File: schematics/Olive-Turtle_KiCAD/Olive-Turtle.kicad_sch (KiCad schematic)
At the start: 12 parts, among them IC1 ENS160-BGLT, U1 ESP32-DEVKITC-32U

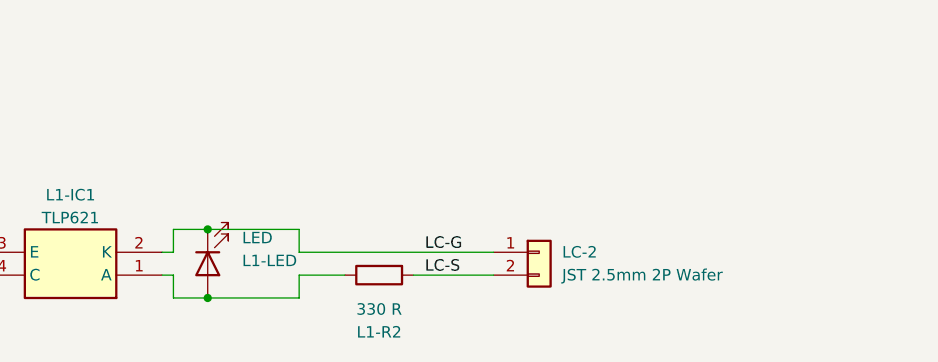
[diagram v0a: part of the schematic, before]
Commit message: [develop] Removed LED from LED Control circuit
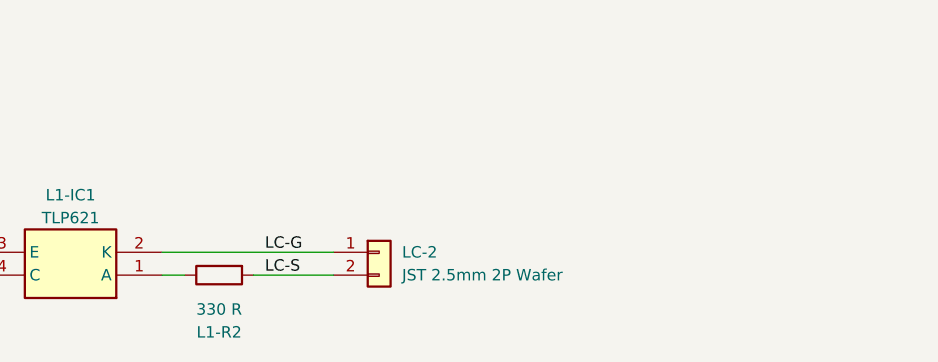
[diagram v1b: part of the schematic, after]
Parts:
- removed L1-LED: LED, symbol Device:LED
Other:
- moved on the sheet: L1-R2, LC-2
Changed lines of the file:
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@@
     (title "Olive Turtle Project - Led Control")
     (date "2023-09-21")
-    (rev "2.1")
+    (rev "2.2")
   )
   (junction (at 191.77 43.18) (diameter 0) (color 0 0 0 0)
   )
-  (junction (at 99.06 156.21) (diameter 0) (color 0 0 0 0)
-  )
   (junction (at 41.91 132.08) (diameter 0) (color 0 0 0 0)
-  )
-  (junction (at 99.06 148.59) (diameter 0) (color 0 0 0 0)
   )
   (junction (at 220.98 68.58) (diameter 0) (color 0 0 0 0)
@@
     (stroke (width 0) (type default))
   )
-  (wire (pts (xy 93.98 153.67) (xy 95.25 153.67))
-    (stroke (width 0) (type default))
-  )
   (wire (pts (xy 44.45 120.65) (xy 44.45 158.75))
     (stroke (width 0) (type default))
@@
     (stroke (width 0) (type default))
   )
-  (wire (pts (xy 114.3 153.67) (xy 109.22 153.67))
+  (wire (pts (xy 93.98 153.67) (xy 96.52 153.67))
     (stroke (width 0) (type default))
   )
@@
     (stroke (width 0) (type default))
   )
-  (wire (pts (xy 95.25 151.13) (xy 95.25 148.59))
-    (stroke (width 0) (type default))
-  )
   (wire (pts (xy 166.37 81.28) (xy 194.31 81.28))
     (stroke (width 0) (type default))
@@
     (stroke (width 0) (type default))
   )
-  (wire (pts (xy 121.92 153.67) (xy 130.81 153.67))
+  (wire (pts (xy 104.14 153.67) (xy 113.03 153.67))
     (stroke (width 0) (type default))
   )
@@
     (stroke (width 0) (type default))
   )
-  (wire (pts (xy 95.25 156.21) (xy 99.06 156.21))
-    (stroke (width 0) (type default))
-  )
-  (wire (pts (xy 130.81 151.13) (xy 109.22 151.13))
+  (wire (pts (xy 93.98 151.13) (xy 113.03 151.13))
     (stroke (width 0) (type default))
   )
@@
     (stroke (width 0) (type default))
   )
-  (wire (pts (xy 109.22 148.59) (xy 99.06 148.59))
-    (stroke (width 0) (type default))
-  )
   (wire (pts (xy 44.45 158.75) (xy 54.61 158.75))
     (stroke (width 0) (type default))
@@
     (stroke (width 0) (type default))
   )
-  (wire (pts (xy 93.98 151.13) (xy 95.25 151.13))
-    (stroke (width 0) (type default))
-  )
   (wire (pts (xy 191.77 43.18) (xy 195.58 43.18))
     (stroke (width 0) (type default))
   )
-  (wire (pts (xy 95.25 148.59) (xy 99.06 148.59))
-    (stroke (width 0) (type default))
-  )
   (wire (pts (xy 115.57 83.82) (xy 125.73 83.82))
     (stroke (width 0) (type default))
@@
     (stroke (width 0) (type default))
   )
-  (wire (pts (xy 109.22 156.21) (xy 99.06 156.21))
-    (stroke (width 0) (type default))
-  )
-  (wire (pts (xy 95.25 153.67) (xy 95.25 156.21))
-    (stroke (width 0) (type default))
-  )
   (wire (pts (xy 125.73 68.58) (xy 125.73 43.18))
     (stroke (width 0) (type default))
   )
-  (wire (pts (xy 109.22 153.67) (xy 109.22 156.21))
-    (stroke (width 0) (type default))
-  )
   (wire (pts (xy 190.5 92.71) (xy 190.5 73.66))
-    (stroke (width 0) (type default))
-  )
-  (wire (pts (xy 109.22 151.13) (xy 109.22 148.59))
     (stroke (width 0) (type default))
   )
@@
     (effects (font (size 1.27 1.27)) (justify right bottom))
   )
-  (label "LC-S" (at 123.19 153.67 0) (fields_autoplaced)
+  (label "LC-S" (at 105.41 153.67 0) (fields_autoplaced)
     (effects (font (size 1.27 1.27)) (justify left bottom))
   )
@@
     (effects (font (size 1.27 1.27)) (justify left bottom))
   )
-  (label "LC-G" (at 123.19 151.13 0) (fields_autoplaced)
+  (label "LC-G" (at 105.41 151.13 0) (fields_autoplaced)
     (effects (font (size 1.27 1.27)) (justify left bottom))
   )
@@
     )
   )
-  (symbol (lib_id "Device:R") (at 118.11 153.67 90) (mirror x) (unit 1)
+  (symbol (lib_id "Device:R") (at 100.33 153.67 90) (mirror x) (unit 1)
     (in_bom yes) (on_board yes) (dnp no) (fields_autoplaced)
-    (property "Reference" "L1-R2" (at 118.11 160.02 90)
-      (effects (font (size 1.27 1.27)))
-    )
-    (property "Value" "330 R" (at 118.11 157.48 90)
-      (effects (font (size 1.27 1.27)))
-    )
-    (property "Footprint" "Resistor_THT:R_Axial_DIN0204_L3.6mm_D1.6mm_P7.62mm_Horizontal" (at 118.11 151.892 90)
-      (effects (font (size 1.27 1.27)) hide)
-    )
-    (property "Datasheet" "~" (at 118.11 153.67 0)
+    (property "Reference" "L1-R2" (at 100.33 160.02 90)
+      (effects (font (size 1.27 1.27)))
+    )
+    (property "Value" "330 R" (at 100.33 157.48 90)
+      (effects (font (size 1.27 1.27)))
+    )
+    (property "Footprint" "Resistor_THT:R_Axial_DIN0204_L3.6mm_D1.6mm_P7.62mm_Horizontal" (at 100.33 151.892 90)
+      (effects (font (size 1.27 1.27)) hide)
+    )
+    (property "Datasheet" "~" (at 100.33 153.67 0)
       (effects (font (size 1.27 1.27)) hide)
     )
@@
     )
   )
-  (symbol (lib_id "Device:LED") (at 99.06 152.4 90) (mirror x) (unit 1)
+  (symbol (lib_id "Connector_Generic:Conn_01x02") (at 118.11 151.13 0) (unit 1)
     (in_bom yes) (on_board yes) (dnp no)
-    (property "Reference" "L1-LED" (at 102.87 152.0825 90)
-      (effects (font (size 1.27 1.27)) (justify right))
-    )
-    (property "Value" "LED" (at 102.87 149.5425 90)
-      (effects (font (size 1.27 1.27)) (justify right))
-    )
-    (property "Footprint" "" (at 99.06 152.4 0)
-      (effects (font (size 1.27 1.27)) hide)
-    )
-    (property "Datasheet" "~" (at 99.06 152.4 0)
-      (effects (font (size 1.27 1.27)) hide)
-    )
-    (pin "1")
-    (pin "2")
-    (instances
-      (project "Olive-Turtle"
-        (path "/51055cea-6c3b-4d6e-9886-de884be04eed"
-          (reference "L1-LED") (unit 1)
-        )
-      )
-    )
-  )
-  (symbol (lib_id "Connector_Generic:Conn_01x02") (at 135.89 151.13 0) (unit 1)
-    (in_bom yes) (on_board yes) (dnp no)
-    (property "Reference" "LC-2" (at 138.43 151.13 0)
+    (property "Reference" "LC-2" (at 120.65 151.13 0)
       (effects (font (size 1.27 1.27)) (justify left))
     )
-    (property "Value" "JST 2.5mm 2P Wafer" (at 138.43 153.67 0)
+    (property "Value" "JST 2.5mm 2P Wafer" (at 120.65 153.67 0)
       (effects (font (size 1.27 1.27)) (justify left))
     )
-    (property "Footprint" "Connector_JST:JST_EH_B2B-EH-A_1x02_P2.50mm_Vertical" (at 135.89 151.13 0)
-      (effects (font (size 1.27 1.27)) hide)
-    )
-    (property "Datasheet" "~" (at 135.89 151.13 0)
-      (effects (font (size 1.27 1.27)) hide)
-    )
+    (property "Footprint" "Connector_JST:JST_EH_B2B-EH-A_1x02_P2.50mm_Vertical" (at 118.11 151.13 0)
+      (effects (font (size 1.27 1.27)) hide)
+    )
+    (property "Datasheet" "~" (at 118.11 151.13 0)
+      (effects (font (size 1.27 1.27)) hide)
+    )

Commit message: [develop] ProtoBoards for all other boards + refactor sch
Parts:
- added POW-1: JST 2.5mm 2P Wafer, Connector_JST:JST_EH_B2B-EH-A_1x02_P2.50mm_Vertical, symbol Connector_Generic:Conn_01x02
- added PROGRAM-1: JST 2.5mm 3P Wafer, symbol Connector_Generic:Conn_01x03
- added SEN-1, SEN-2, SEN-DAISY-1: JST 2.5mm 4P Wafer, symbol Connector_Generic:Conn_01x04
- renumbered A1 to S-1, IC1 to S-2
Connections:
- net LC1-G is gone; now on net GND: LC-1.1 (Pin_1), U1.14 (GND1)
- net GND: now also S-1.2 (GND), S-2.8 (VSS_1), U1.32 (GND2), U1.38 (GND3), POW-1.1 (Pin_1), PROGRAM-1.3 (Pin_3), SEN-1.1 (Pin_1), SEN-2.1 (Pin_1), SEN-DAISY-1.1 (Pin_1)
- net SCL: now also SEN-1.4 (Pin_4), SEN-2.4 (Pin_4), SEN-DAISY-1.4 (Pin_4)
- net SDA: now also SEN-1.3 (Pin_3), SEN-2.3 (Pin_3), SEN-DAISY-1.3 (Pin_3)
- net 3V3: now reaches S-1.1 (VCC), S-2.5 (VDDIO), U1.1 (3V3)
- net 3V3: now also SEN-1.2 (Pin_2), SEN-2.2 (Pin_2), SEN-DAISY-1.2 (Pin_2)
- net 5V IN: now reaches U1.19 (EXT_5V)
- net 5V IN: now also POW-1.2 (Pin_2)
- net RX: now reaches U1.34 (RXD0)
- net RX: now also PROGRAM-1.2 (Pin_2)
- net TX: now reaches U1.35 (TXD0)
- net TX: now also PROGRAM-1.1 (Pin_1)
- no-connect marks 39 -> 35
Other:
- note added: "LC Line"
- note added: "Led Control ProtoBoard"
- note added: "Main board ProtoBoard"
- note added: "SEN Line"
- note added: "Sensors ProtoBoard"
- moved on the sheet: L-IN1, L1-IC1, L1-OUT1, L1-R1, L1-R2, L1-T1, LC-1, LC-2, S-1, S-2, U1
